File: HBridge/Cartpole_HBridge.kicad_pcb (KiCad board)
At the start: 2 copper layers, 36.5 x 22 mm, 14 parts, among them J1 Conn_01x12_Pin, J2 Barrel_Jack, J3 Conn_01x06_Socket, Q1 BSS84P, U1 TB6612FNG

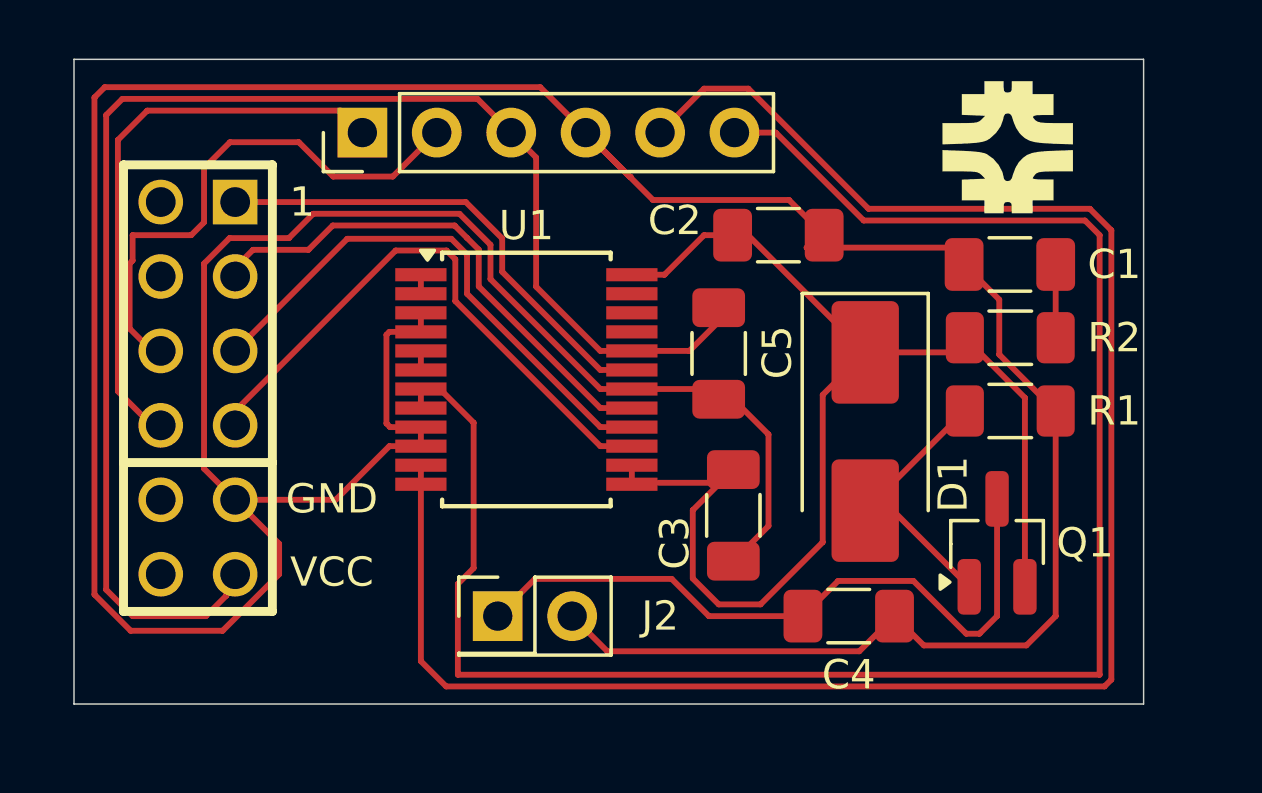
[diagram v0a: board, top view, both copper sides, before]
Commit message: Upped the footprint size of the 470uf cap
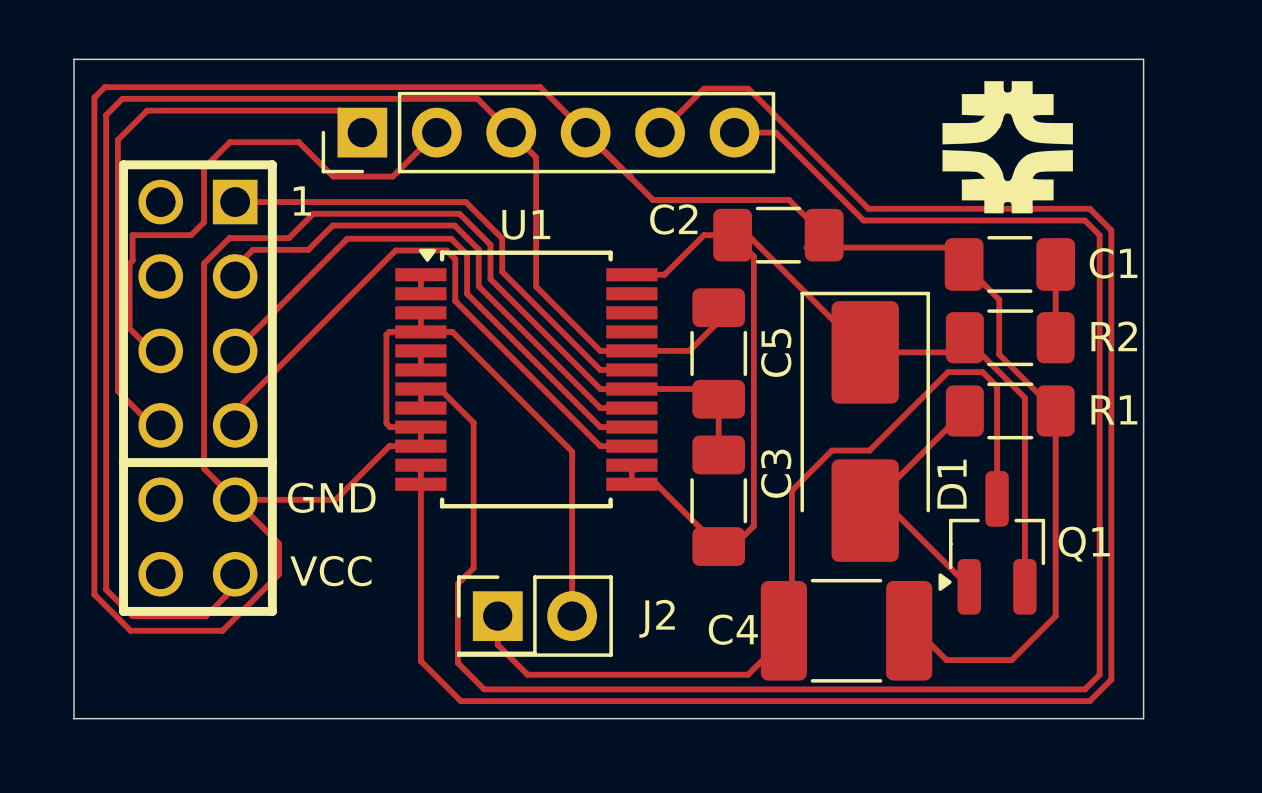
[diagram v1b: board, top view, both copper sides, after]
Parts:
- C4: footprint Capacitor_SMD:C_1206_3216Metric_Pad1.33x1.80mm_HandSolder -> Capacitor_SMD:C_1812_4532Metric_Pad1.57x3.40mm_HandSolder
- moved C3 0.71 mm to (65.5, 69.6), turned to 90 degrees
- moved C4 0.51 mm to (69.9, 74.0)
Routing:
- net Net-(Q1-D): track 23.6 -> 29.6 mm
- net GND: track 145.1 -> 140.4 mm
- net Net-(D1-K): track 44.6 -> 40.0 mm
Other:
- board size 36.5 x 22 mm -> 36.5 x 22.5 mm

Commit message: Changed 470uf cap to one more readily availible
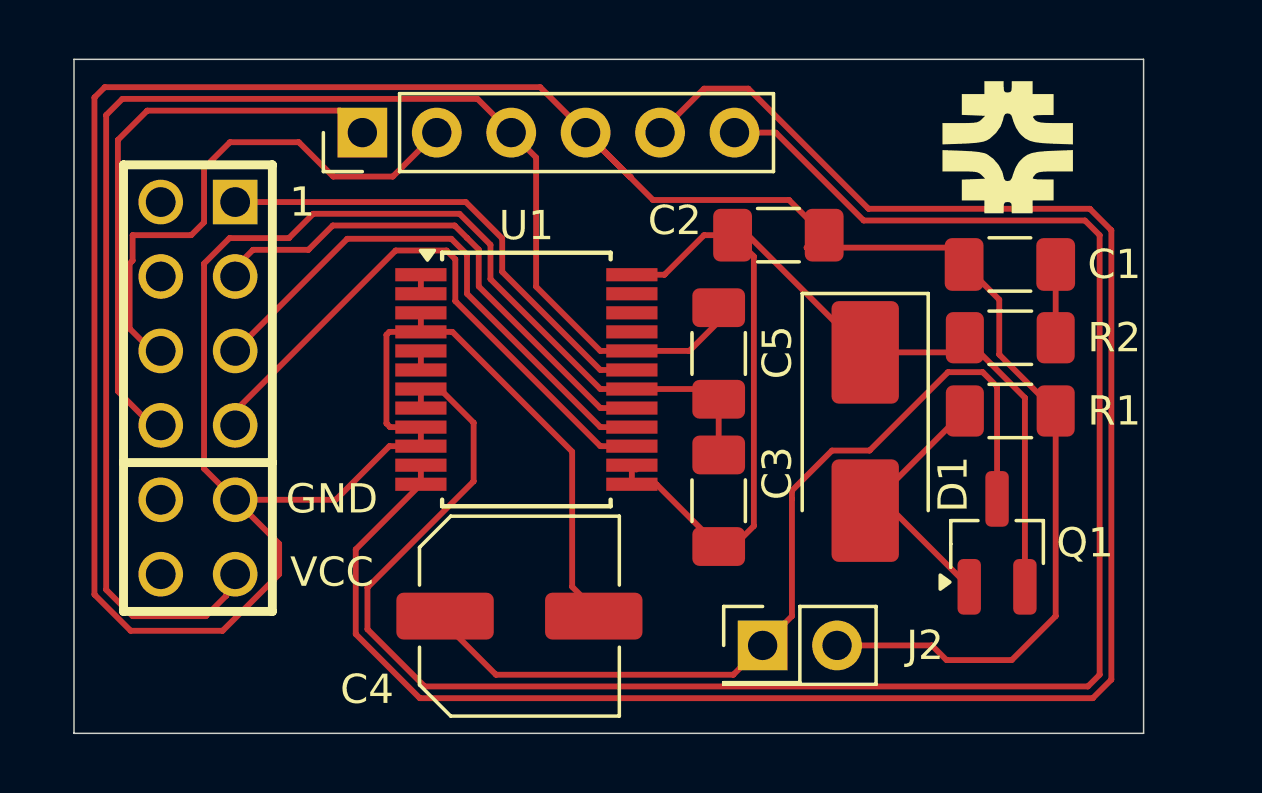
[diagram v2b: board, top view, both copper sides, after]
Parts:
- C4: footprint Capacitor_SMD:C_1812_4532Metric_Pad1.57x3.40mm_HandSolder -> Capacitor_SMD:C_Elec_6.3x7.7
- moved C4 11.2 mm to (58.7, 73.5)
- moved J2 9.10 mm to (67.0, 74.5)
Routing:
- net Net-(J3-Pin_6): track 62.7 -> 66.3 mm
- net GND: track 140.4 -> 143.4 mm
- net Net-(J3-Pin_5): track 64.5 -> 67.0 mm
- net Net-(Q1-D): track 29.6 -> 30.8 mm
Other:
- board size 36.5 x 22.5 mm -> 36.5 x 23 mm

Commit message: Compressed size of board to be within PMod spec
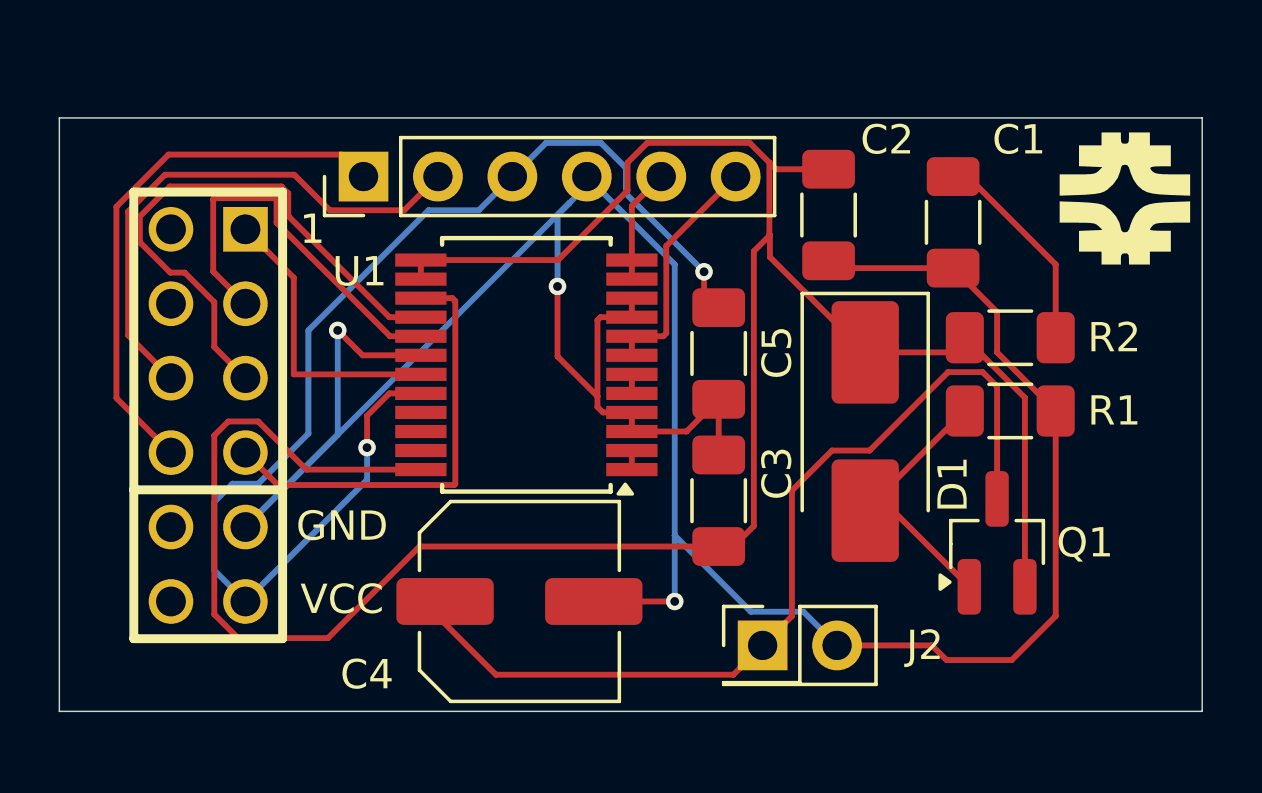
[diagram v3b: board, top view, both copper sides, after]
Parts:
- C1: value 10 -> 10 uf
- C2, C5: value 0.1 -> 0.1 uf
- C3: value 0.47 -> 0.47 uf
- C4: value 470 -> 470 uf
- D1: value 6.8 V -> 6.8 V Zener
- J1: value Conn_01x12_Pin -> PMod Connector
- R1: value 100k -> 100K
- R2: value 1 -> 1R
- moved G*** 4.37 mm to (79.5, 59.2)
- moved C1 2.41 mm to (73.5, 60.1), turned to -90 degrees
- moved C2 1.85 mm to (69.2, 59.8), turned to -90 degrees
- moved J3 1.50 mm to (53.4, 58.5)
- moved J1 0.99 mm to (48.1, 66.7)
- moved C4 0.50 mm to (58.7, 73.0)
- moved U1 0.50 mm to (58.9, 64.9), turned to 180 degrees
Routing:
- net Net-(J3-Pin_5): track 67.0 -> 3.92 mm
- net Net-(J3-Pin_6): track 66.3 -> 8.20 mm
- net GND: track 143.4 -> 99.1 mm, vias 0 -> 3
- net Net-(D1-K): track 40.0 -> 82.7 mm
- net VCC: track 49.9 -> 41.7 mm, vias 0 -> 2
- net Net-(J1-Pin_1): track 16.9 -> 9.97 mm
- net Net-(J1-Pin_4): track 19.9 -> 15.1 mm
- net Net-(C1-Pad1): track 2.50 -> 7.24 mm
- net Net-(J1-Pin_2): track 17.9 -> 13.6 mm
- net Net-(D1-A): track 11.7 -> 9.44 mm
- net Net-(J1-Pin_3): track 18.7 -> 19.6 mm
- net Net-(J1-Pin_10): track 19.3 -> 18.6 mm
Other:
- board size 36.5 x 23 mm -> 39 x 20.2 mm

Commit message: Made the board somewhat smaller and more compressed
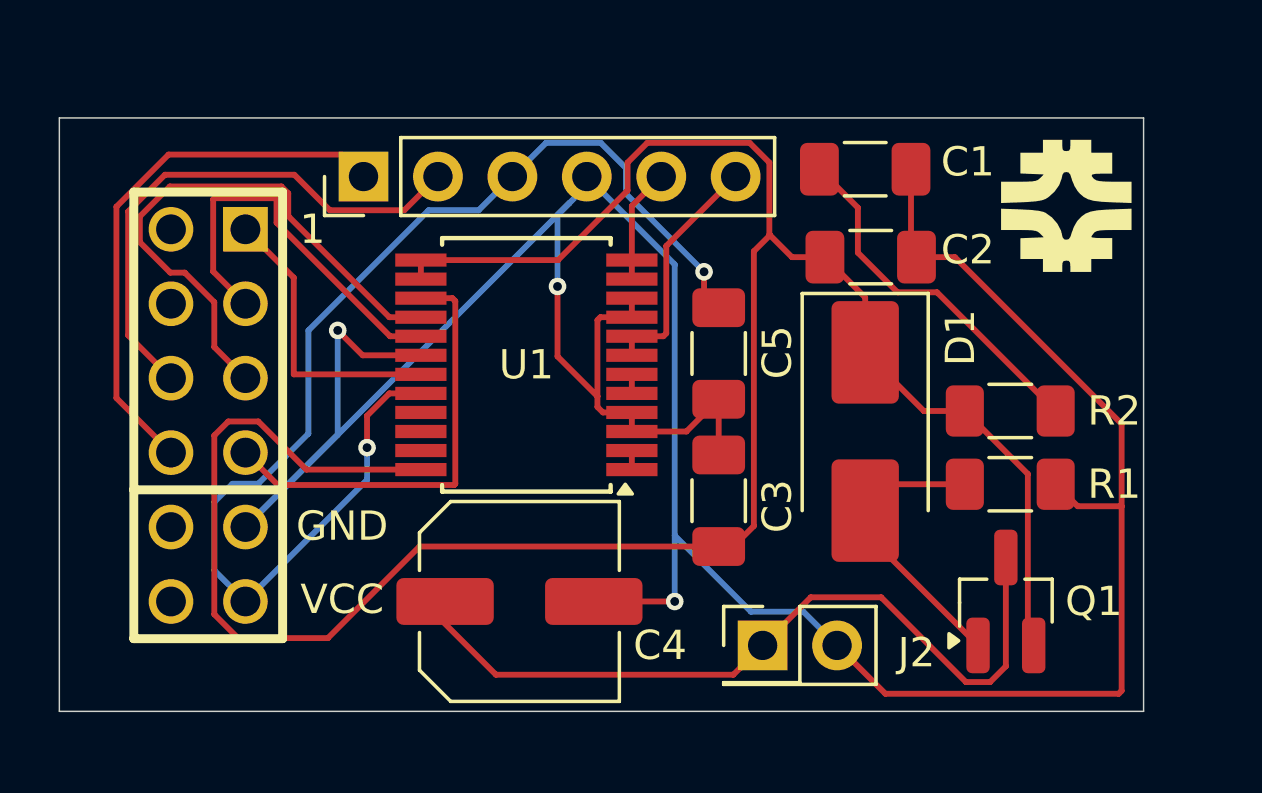
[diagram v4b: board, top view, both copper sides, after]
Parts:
- moved C1 3.51 mm to (70.5, 58.2), turned to 0 degrees
- moved R1 2.50 mm to (75.5, 69.0)
- moved R2 2.50 mm to (75.5, 66.5)
- moved C2 2.03 mm to (70.7, 61.2), turned to 0 degrees
- moved Q1 2.02 mm to (75.3, 73.0)
- moved G*** 2.02 mm to (77.5, 59.5)
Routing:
- net GND: track 99.1 -> 107.6 mm
- net Net-(C1-Pad1): track 7.24 -> 12.4 mm
- net Net-(Q1-D): track 30.8 -> 26.5 mm
- net Net-(D1-A): track 9.44 -> 10.9 mm
- net Net-(D1-K): track 82.7 -> 81.5 mm
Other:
- board size 39 x 20.2 mm -> 37 x 20.2 mm
